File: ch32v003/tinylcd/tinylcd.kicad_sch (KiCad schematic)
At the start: 5 parts, among them U1 RB017A1505A_Connector

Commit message: Bump versions.
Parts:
- removed C?: 10u, Capacitor_SMD:C_0402_1005Metric, symbol Device:C
- removed R? (x2): 0, Resistor_SMD:R_0402_1005Metric, symbol Device:R
- added C1: 1u, Resistor_SMD:R_0402_1005Metric, symbol Device:C
- added C2, C3: 4.7u, Resistor_SMD:R_0402_1005Metric, symbol Device:C
- added J1: APPLE, artwork:apple, symbol artwork:artwork
- added J2: USB_C_Receptacle_USB2.0, Connector_USB:USB_C_Receptacle_HRO_TYPE-C-31-M-12, symbol Connector:USB_C_Receptacle_USB2.0
- added J3: PGM, Connector_PinHeader_2.54mm:PinHeader_1x04_P2.54mm_Vertical, symbol Connector_Generic:Conn_01x04
- added R1: 4.99, Resistor_SMD:R_0603_1608Metric, symbol Device:R
- added R2, R3: 5.1k, Resistor_SMD:R_0402_1005Metric, symbol Device:R
- added U2: 25WQ32, cnhardware:USON8-LINE(2x3), symbol Memory_Flash:W25Q32JVZP
- added U4: 3.3vReg, cnhardware:xdfn-reg, symbol Regulator_Linear:NCP115AMX120TCG
- gave numbers to parts that had none: 1
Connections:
- net LCD18 is gone; now on net VDD: U1.2 (VCC1.8V)
- net LCD28 is gone; now on net VDD: U1.10 (VDD2.8V)
- net GND: now also C1.1, C2.1, C3.1, J2.A1 (GND), J2.A12 (GND), J2.B1 (GND), J2.B12 (GND), J2.S1 (SHIELD), J3.1 (Pin_1), R2.2, R3.2, U2.4 (GND), U2.9 (EP), U4.2 (GND), U4.5 (GND)
- net TFT_CS: now also U3.19 (PD5/A5/UTX/T2CH4/URX); no longer U3.16 (PD2/A3/T1CH1/T2CH3/T1CH2N)
- net TFT_FMARK: now also U3.17 (PD3/A4/T2CH2/AETR/UCTS/T1CH4); no longer U3.19 (PD5/A5/UTX/T2CH4/URX)
- net TFT_LEDA: now also R1.1
- net TFT_RESET: now also U3.16 (PD2/A3/T1CH1/T2CH3/T1CH2N); no longer U3.17 (PD3/A4/T2CH2/AETR/UCTS/T1CH4)
- net VDD: now also C1.2, C2.2, J3.3 (Pin_3), R1.2, U2.8 (VCC), U4.1 (OUT)
- net D-: now reaches U3.1 (PD7/NRST/T2CH4/OPP1/UCK)
- net D-: now also J2.A7 (D-), J2.B7 (D-)
- net FIOB: now reaches U3.10 (PC3/T1CH3/T1CHIN/UCTS)
- net FIOB: now also U2.7 (IO3)
- net SCK: now reaches U3.11 (PC4/A2/T1CH4/MCO/T1CH1CH2N)
- net SCK: now also U2.6 (CLK)
- net SS: now reaches U3.14 (PC7/MISO/T1CH2/T2CH2/URTS)
- net SS: now also U2.1 (~{CS})
- net SWIO: now reaches U3.15 (PD1/SWIO/AETR/T1CH3/SCL/URX)
- net SWIO: now also J3.2 (Pin_2)
- net D+: now reaches U3.2 (PA1/OSCI/A1/T1CH2/OPN0)
- net D+: now also J2.A6 (D+), J2.B6 (D+)
- net SBU2: now reaches U3.20 (PD6/A7/URX/T2CH3/UTX)
- net SBU2: now also J2.B8 (SBU2)
- net SBU1: now reaches U3.3 (PA2/OSCO/A0/T1CH2N/OPP0/AETR2)
- net SBU1: now also J2.A8 (SBU1)
- net PD0: now reaches U3.5 (PD0/T1CH1N/OPN1/SDA/UTX)
- net PD0: now also J3.4 (Pin_4)
- net MOSI: now reaches U3.7 (PC0/T2CH3/UTX/NSS/T1CH3)
- net MOSI: now also U2.5 (DI(IO0))
- net MISO: now reaches U3.8 (PC1/SDA/NSS/T2CH4/T2CH1ETR/T1BKIN/URX)
- net MISO: now also U2.2 (DO(IO1))
- net FIOA: now reaches U3.9 (PC2/SCL/URTS/T1BKIN/AETR/T2CH2/T1ETR)
- net FIOA: now also U2.3 (IO2)
- new net: J2.B5 (CC2), R3.1
- new net: J2.A5 (CC1), R2.1
- new net +5V: C3.2, J2.A4 (VBUS), J2.A9 (VBUS), J2.B4 (VBUS), J2.B9 (VBUS), U4.3 (EN), U4.4 (IN)
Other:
- note removed: "Is 8Mbit ok?"
- moved on the sheet: U1

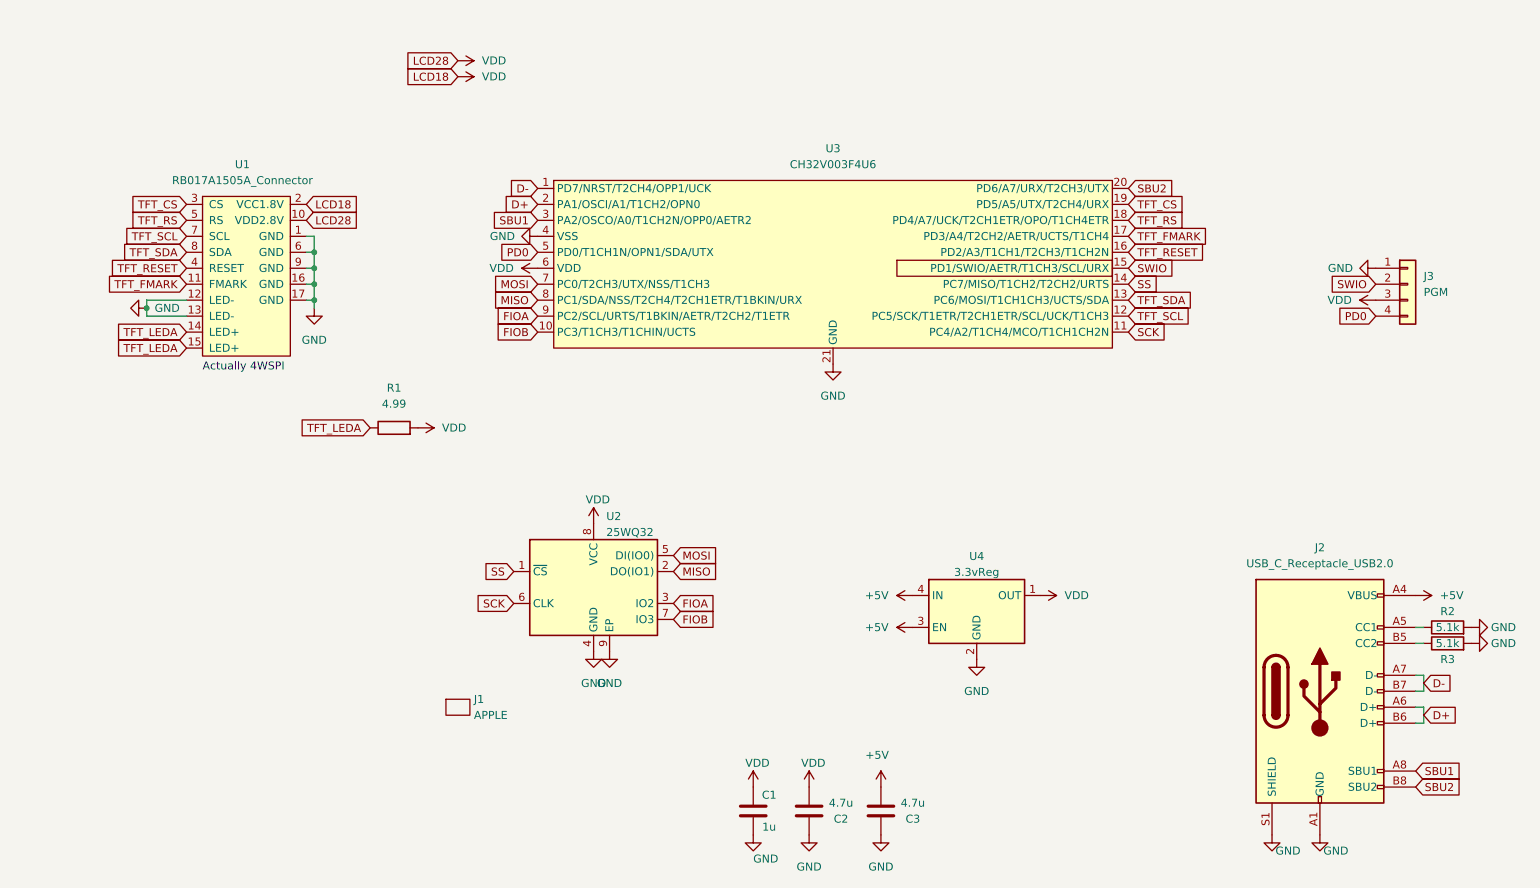
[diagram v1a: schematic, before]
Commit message: Add parts + Update tinylcd.
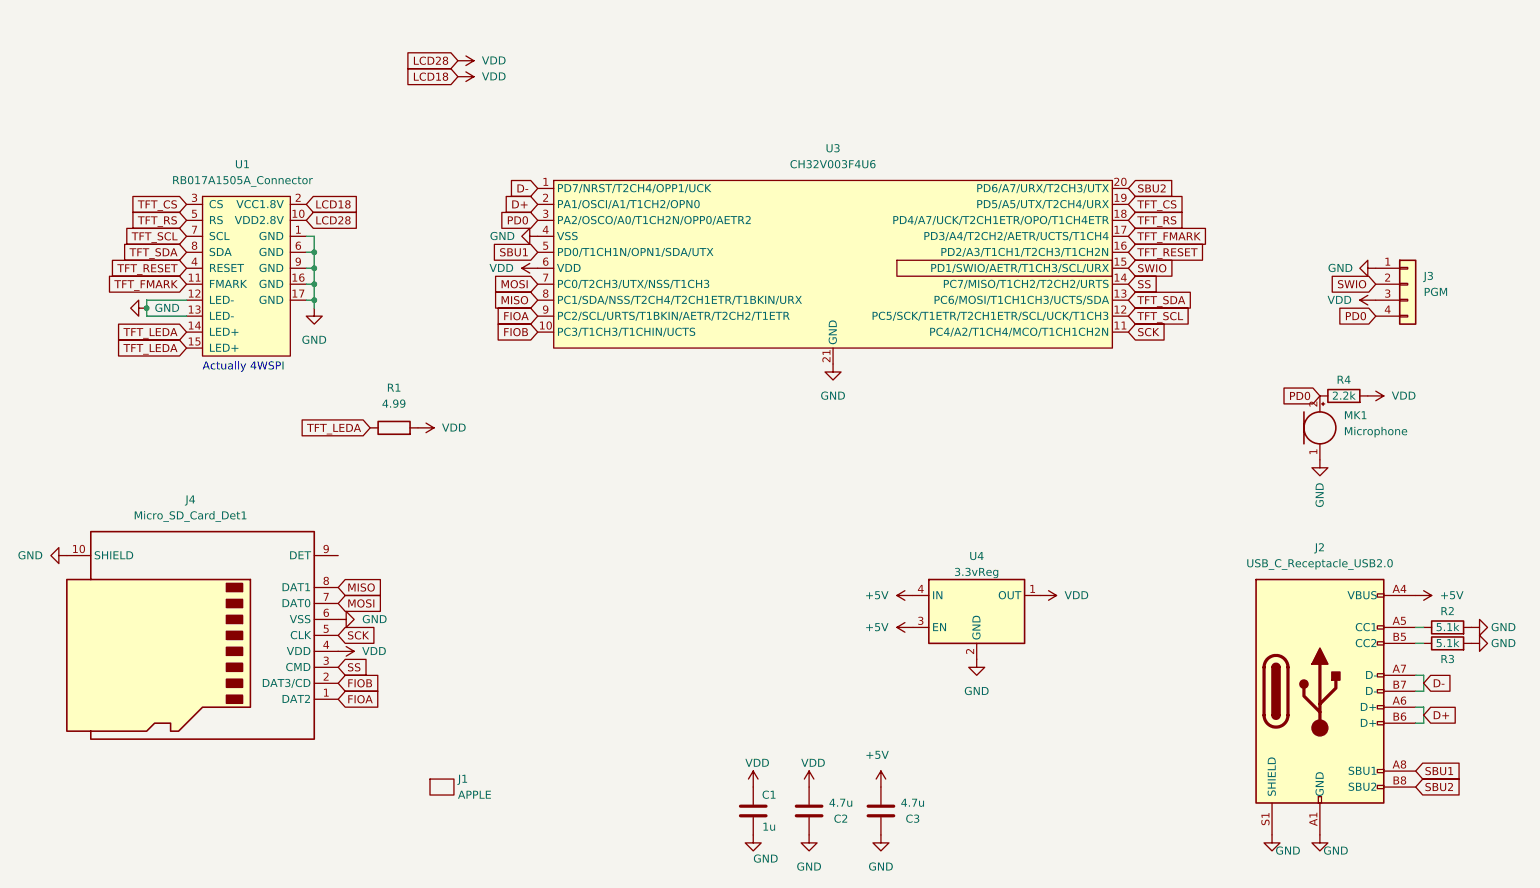
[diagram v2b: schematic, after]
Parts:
- removed U2: 25WQ32, cnhardware:USON8-LINE(2x3), symbol Memory_Flash:W25Q32JVZP
- added J4: Micro_SD_Card_Det1, cnhardware:MicroSD-C393941-SHOU-HAN-TF-PUSH, symbol Connector:Micro_SD_Card_Det1
- added MK1: Microphone, cnhardware:GOERTEK_MIC_B4013AM423, symbol Device:Microphone
- added R4: 2.2k, Resistor_SMD:R_0402_1005Metric, symbol Device:R
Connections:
- net FIOA: now also J4.1 (DAT2)
- net FIOB: now also J4.2 (DAT3/CD)
- net GND: now also J4.10 (SHIELD), J4.6 (VSS), MK1.1 (-)
- net MISO: now also J4.8 (DAT1)
- net MOSI: now also J4.7 (DAT0)
- net PD0: now also U3.3 (PA2/OSCO/A0/T1CH2N/OPP0/AETR2), MK1.2 (+), R4.1; no longer U3.5 (PD0/T1CH1N/OPN1/SDA/UTX)
- net SBU1: now also U3.5 (PD0/T1CH1N/OPN1/SDA/UTX); no longer U3.3 (PA2/OSCO/A0/T1CH2N/OPP0/AETR2)
- net SCK: now also J4.5 (CLK)
- net SS: now also J4.3 (CMD)
- net VDD: now also J4.4 (VDD), R4.2
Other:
- moved on the sheet: J1

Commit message: Update design
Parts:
- added R5: 1.5k, Resistor_SMD:R_0402_1005Metric, symbol Device:R
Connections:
- net D-: now also R5.2
- net VDD: now also R5.1
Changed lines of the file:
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@@
+    )
+  )
+  (global_label "D-" (shape input) (at 248.92 43.18 0) (fields_autoplaced)
+    (effects (font (size 1.27 1.27)) (justify left))
+    (property "Intersheetrefs" "${INTERSHEET_REFS}" (at 254.1755 43.1006 0)
+      (effects (font (size 1.27 1.27)) (justify left) hide)
     )
   )
@@
         (path "/e63e39d7-6ac0-4ffd-8aa3-1841a4541b55"
           (reference "#PWR0108") (unit 1)
+        )
+      )
+    )
+  )
+  (symbol (lib_id "power:VDD") (at 241.3 43.18 90) (unit 1)
+    (in_bom yes) (on_board yes) (dnp no) (fields_autoplaced)
+    (property "Reference" "#PWR06" (at 245.11 43.18 0)
+      (effects (font (size 1.27 1.27)) hide)
+    )
+    (property "Value" "VDD" (at 237.49 43.1799 90)
+      (effects (font (size 1.27 1.27)) (justify left))
+    )
+    (property "Footprint" "" (at 241.3 43.18 0)
+      (effects (font (size 1.27 1.27)) hide)
+    )
+    (property "Datasheet" "" (at 241.3 43.18 0)
+      (effects (font (size 1.27 1.27)) hide)
+    )
+    (pin "1")
+    (instances
+      (project "tinylcd"
+        (path "/e63e39d7-6ac0-4ffd-8aa3-1841a4541b55"
+          (reference "#PWR06") (unit 1)
         )
       )
@@
         )
       )
+    )
+  )
+  (symbol (lib_id "Device:R") (at 245.11 43.18 90) (unit 1)
+    (in_bom yes) (on_board yes) (dnp no)
+    (property "Reference" "R5" (at 245.11 45.72 90)
+      (effects (font (size 1.27 1.27)))
+    )
+    (property "Value" "1.5k" (at 245.11 43.18 90)
+      (effects (font (size 1.27 1.27)))
+    )
+    (property "Footprint" "Resistor_SMD:R_0402_1005Metric" (at 245.11 44.958 90)
+      (effects (font (size 1.27 1.27)) hide)
+    )
+    (property "Datasheet" "~" (at 245.11 43.18 0)
+      (effects (font (size 1.27 1.27)) hide)
+    )
+    (property "LCSC" "C25867" (at 245.11 43.18 0)
+      (effects (font (size 1.27 1.27)) hide)
+    )
+    (pin "1")
+    (pin "2")
+    (instances
+      (project "tinylcd"
+        (path "/e63e39d7-6ac0-4ffd-8aa3-1841a4541b55"
+          (reference "R5") (unit 1)
+        )
+      )

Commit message: Oops a few fixes.
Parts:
- J3: LCSC (none) -> NP
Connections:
- net D+: now also U3.1 (PD7/NRST/T2CH4/OPP1/UCK); no longer U3.2 (PA1/OSCI/A1/T1CH2/OPN0)
- net D-: now also U3.20 (PD6/A7/URX/T2CH3/UTX); no longer U3.1 (PD7/NRST/T2CH4/OPP1/UCK)
- net SBU2: now also U3.2 (PA1/OSCI/A1/T1CH2/OPN0); no longer U3.20 (PD6/A7/URX/T2CH3/UTX)
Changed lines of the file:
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@@
-    )
-  )
-  (global_label "D-" (shape input) (at 97.79 52.07 180) (fields_autoplaced)
-    (effects (font (size 1.27 1.27)) (justify right))
-    (property "Intersheetrefs" "${INTERSHEET_REFS}" (at 92.5345 51.9906 0)
-      (effects (font (size 1.27 1.27)) (justify right) hide)
     )
   )
@@
     )
   )
+  (global_label "SBU2" (shape input) (at 97.79 54.61 180) (fields_autoplaced)
+    (effects (font (size 1.27 1.27)) (justify right))
+    (property "Intersheetrefs" "${INTERSHEET_REFS}" (at 89.7853 54.61 0)
+      (effects (font (size 1.27 1.27)) (justify right) hide)
+    )
+  )
   (global_label "SCK" (shape input) (at 66.04 123.19 0) (fields_autoplaced)
     (effects (font (size 1.27 1.27)) (justify left))
@@
     )
   )
+  (global_label "D+" (shape input) (at 97.79 52.07 180) (fields_autoplaced)
+    (effects (font (size 1.27 1.27)) (justify right))
+    (property "Intersheetrefs" "${INTERSHEET_REFS}" (at 91.9624 52.07 0)
+      (effects (font (size 1.27 1.27)) (justify right) hide)
+    )
+  )
   (global_label "TFT_LEDA" (shape input) (at 41.91 74.93 180) (fields_autoplaced)
     (effects (font (size 1.27 1.27)) (justify right))
@@
     )
   )
-  (global_label "D+" (shape input) (at 97.79 54.61 180) (fields_autoplaced)
-    (effects (font (size 1.27 1.27)) (justify right))
-    (property "Intersheetrefs" "${INTERSHEET_REFS}" (at 92.5345 54.5306 0)
-      (effects (font (size 1.27 1.27)) (justify right) hide)
-    )
-  )
   (global_label "LCD28" (shape input) (at 60.96 57.15 0) (fields_autoplaced)
     (effects (font (size 1.27 1.27)) (justify left))
@@
     )
   )
-  (global_label "SBU2" (shape input) (at 191.77 52.07 0) (fields_autoplaced)
-    (effects (font (size 1.27 1.27)) (justify left))
-    (property "Intersheetrefs" "${INTERSHEET_REFS}" (at 199.2026 51.9906 0)
-      (effects (font (size 1.27 1.27)) (justify left) hide)
-    )
-  )
   (global_label "TFT_CS" (shape input) (at 41.91 54.61 180) (fields_autoplaced)
     (effects (font (size 1.27 1.27)) (justify right))
@@
     (property "Intersheetrefs" "${INTERSHEET_REFS}" (at 29.7602 64.6906 0)
       (effects (font (size 1.27 1.27)) (justify right) hide)
+    )
+  )
+  (global_label "D-" (shape input) (at 191.77 52.07 0) (fields_autoplaced)
+    (effects (font (size 1.27 1.27)) (justify left))
+    (property "Intersheetrefs" "${INTERSHEET_REFS}" (at 197.5976 52.07 0)
+      (effects (font (size 1.27 1.27)) (justify left) hide)
     )
   )
@@
       (effects (font (size 1.27 1.27)) hide)
     )
+    (property "LCSC" "NP" (at 236.22 67.31 0)
+      (effects (font (size 1.27 1.27)) hide)
+    )

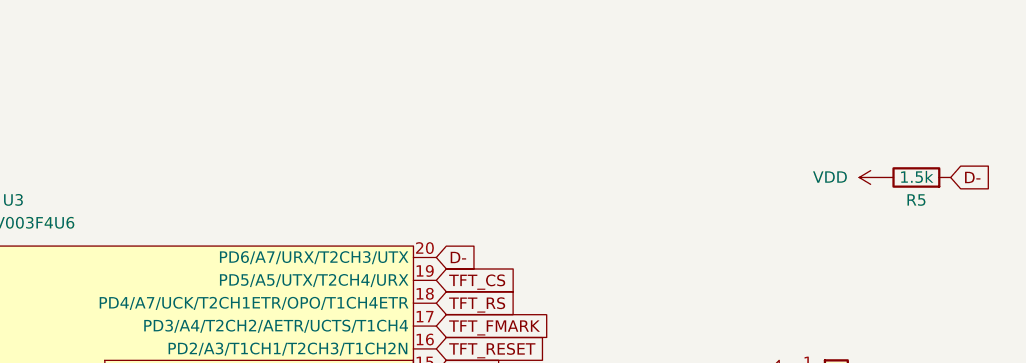
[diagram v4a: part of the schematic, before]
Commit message: Update with notes and a new design to test the LCD displays.
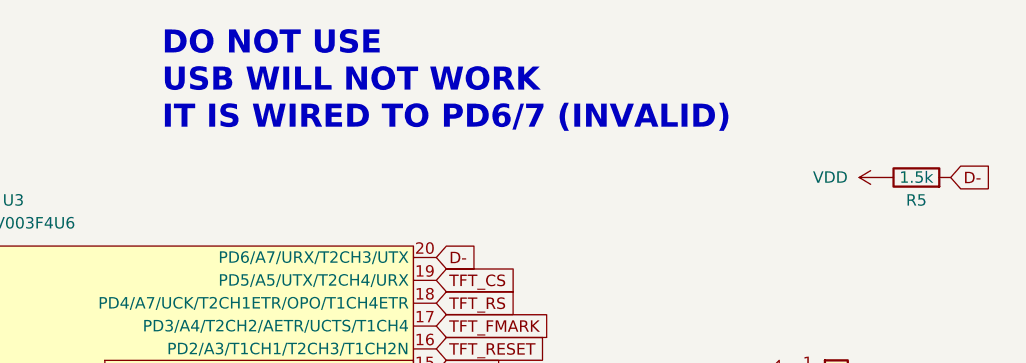
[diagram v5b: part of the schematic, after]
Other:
- note added: "DO NOT USE USB WILL NOT WORK IT IS WIRED TO PD6/7 (INVALID)"
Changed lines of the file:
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@@
     (effects (font (size 1.27 1.27)) (justify left bottom))
+  )
+  (text "DO NOT USE\nUSB WILL NOT WORK\nIT IS WIRED TO PD6/7 (INVALID)"
+    (at 161.29 38.1 0)
+    (effects (font (size 2.56 2.56) (thickness 0.512) bold) (justify left bottom))
   )
   (global_label "TFT_CS" (shape input) (at 191.77 54.61 0) (fields_autoplaced)
